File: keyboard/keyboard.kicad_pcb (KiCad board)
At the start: 2 copper layers, 214.3 x 114.3 mm, 67 parts, among them SW1 MX_SW_HS, SW10 MX_SW_HS, SW11 MX_SW_HS, SW12 MX_SW_HS, SW13 MX_SW_HS, SW14 MX_SW_HS, SW15 MX_SW_HS, SW16 MX_SW_HS, SW17 MX_SW_HS, SW18 MX_SW_HS, SW19 MX_SW_HS, SW2 MX_SW_HS, SW20 MX_SW_HS, SW21 MX_SW_HS, SW22 MX_SW_HS, SW23 MX_SW_HS, SW24 MX_SW_HS, SW25 MX_SW_HS, SW26 MX_SW_HS, SW27 MX_SW_HS, SW28 MX_SW_HS, SW29 MX_SW_HS, SW3 MX_SW_HS, SW30 MX_SW_HS, SW31 MX_SW_HS, SW32 MX_SW_HS, SW33 MX_SW_HS, SW34 MX_SW_HS, SW35 MX_SW_HS, SW36 MX_SW_HS, SW37 MX_SW_HS, SW38 MX_SW_HS, SW39 MX_SW_HS, SW4 MX_SW_HS, SW40 MX_SW_HS, SW41 MX_SW_HS, SW42 MX_SW_HS, SW43 MX_SW_HS, SW44 MX_SW_HS, SW45 MX_SW_HS, SW46 MX_SW_HS, SW47 MX_SW_HS, SW48 MX_SW_HS, SW49 MX_SW_HS, SW5 MX_SW_HS, SW50 MX_SW_HS, SW51 MX_SW_HS, SW52 MX_SW_HS, SW53 MX_SW_HS, SW54 MX_SW_HS, SW55 MX_SW_HS, SW56 MX_SW_HS, SW57 MX_SW_HS, SW58 MX_SW_HS, SW59 MX_SW_HS, SW6 MX_SW_HS, SW60 MX_SW_HS, SW61 MX_SW_HS, SW62 MX_SW_HS, SW63 MX_SW_HS, SW64 MX_SW_HS, SW7 MX_SW_HS, SW8 MX_SW_HS, SW9 MX_SW_HS, U1 ProMicro

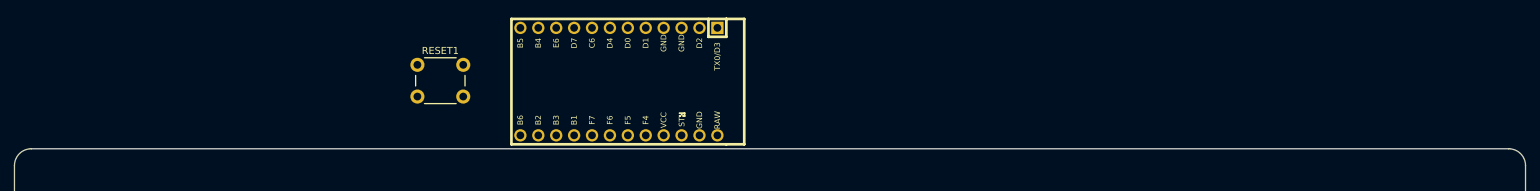
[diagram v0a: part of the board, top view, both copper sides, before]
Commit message: Add reset and cutout for the power switch
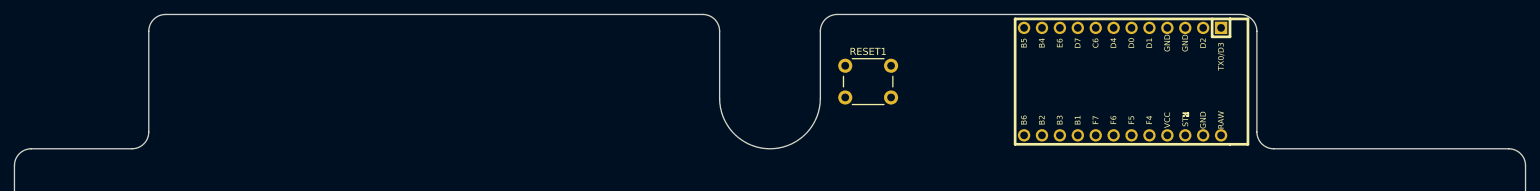
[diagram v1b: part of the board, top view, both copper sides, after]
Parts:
- moved U1 71.4 mm to (197.6, 35.7)
- moved RESET1 60.7 mm to (158.3, 33.5)
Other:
- board size 214.3 x 114.3 mm -> 214.3 x 133.3 mm
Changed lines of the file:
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@@
     )
   )
-  (footprint "Button_Switch_THT:SW_PUSH_6mm_H13mm" (layer "F.Cu")
-    (at 97.63125 33.3375)
+  (footprint "Button_Switch_THT:SW_PUSH_6mm_H13mm" locked (layer "F.Cu")
+    (at 158.309314 33.46875)
     (descr "tactile push button, 6x6mm e.g. PHAP33xx series, height=13mm")
     (tags "tact sw push 6mm")
@@
     (fp_line (start 0.25 5.25) (end 0.25 -0.75) (layer "F.Fab") (width 0.1))
     (fp_circle (center 3.25 2.25) (end 1.25 2.5) (layer "F.Fab") (width 0.1) (fill none))
-    (pad "1" thru_hole circle (at 6.5 0 90) (size 2 2) (drill 1.1) (layers *.Cu *.Mask)
+    (pad "1" thru_hole circle locked (at 6.5 0 90) (size 2 2) (drill 1.1) (layers *.Cu *.Mask)
       (net 152 "unconnected-(RESET1-Pad1)") (pinfunction "1") (pintype "passive"))
-    (pad "1" thru_hole circle (at 0 0 90) (size 2 2) (drill 1.1) (layers *.Cu *.Mask)
+    (pad "1" thru_hole circle locked (at 0 0 90) (size 2 2) (drill 1.1) (layers *.Cu *.Mask)
       (net 152 "unconnected-(RESET1-Pad1)") (pinfunction "1") (pintype "passive"))
-    (pad "2" thru_hole circle (at 6.5 4.5 90) (size 2 2) (drill 1.1) (layers *.Cu *.Mask)
+    (pad "2" thru_hole circle locked (at 6.5 4.5 90) (size 2 2) (drill 1.1) (layers *.Cu *.Mask)
       (net 153 "RESET") (pinfunction "2") (pintype "passive"))
-    (pad "2" thru_hole circle (at 0 4.5 90) (size 2 2) (drill 1.1) (layers *.Cu *.Mask)
+    (pad "2" thru_hole circle locked (at 0 4.5 90) (size 2 2) (drill 1.1) (layers *.Cu *.Mask)
       (net 153 "RESET") (pinfunction "2") (pintype "passive"))
     (model "${KICAD6_3DMODEL_DIR}/Button_Switch_THT.3dshapes/SW_PUSH_6mm_H13mm.wrl"
@@
   )
   (footprint "Keebio-Parts:ArduinoProMicro" (layer "F.Cu")
-    (at 126.20625 35.71875 180)
+    (at 197.64375 35.71875 180)
     (property "Sheetfile" "keyboard.kicad_sch")
     (property "Sheetname" "")
@@
   )
   (gr_line (start 40.48125 47.625) (end 40.48125 157.1625) (layer "Edge.Cuts") (width 0.1))
+  (gr_arc (start 59.53125 42.8625) (mid 58.833798 44.546298) (end 57.15 45.24375) (layer "Edge.Cuts") (width 0.1))
+  (gr_line (start 216.69375 42.8625) (end 216.69375 28.575) (layer "Edge.Cuts") (width 0.1))
+  (gr_arc (start 154.78125 38.1) (mid 147.6375 45.24375) (end 140.49375 38.1) (layer "Edge.Cuts") (width 0.1))
   (gr_line (start 254.79375 157.1625) (end 254.79375 47.625) (layer "Edge.Cuts") (width 0.1))
   (gr_arc (start 252.4125 45.24375) (mid 254.096283 45.941217) (end 254.79375 47.625) (layer "Edge.Cuts") (width 0.1))
@@
   (gr_arc (start 254.79375 157.1625) (mid 254.096283 158.846283) (end 252.4125 159.54375) (layer "Edge.Cuts") (width 0.1))
   (gr_arc (start 40.48125 47.625) (mid 41.178717 45.941217) (end 42.8625 45.24375) (layer "Edge.Cuts") (width 0.1))
+  (gr_line (start 140.49375 28.575) (end 140.49375 38.1) (layer "Edge.Cuts") (width 0.1))
+  (gr_line (start 214.3125 26.19375) (end 157.1625 26.19375) (layer "Edge.Cuts") (width 0.1))
+  (gr_arc (start 59.53125 28.575) (mid 60.228702 26.891202) (end 61.9125 26.19375) (layer "Edge.Cuts") (width 0.1))
+  (gr_line (start 59.53125 42.8625) (end 59.53125 28.575) (layer "Edge.Cuts") (width 0.1))
+  (gr_line (start 57.15 45.24375) (end 42.8625 45.24375) (layer "Edge.Cuts") (width 0.1))
+  (gr_arc (start 214.3125 26.19375) (mid 215.996298 26.891202) (end 216.69375 28.575) (layer "Edge.Cuts") (width 0.1))
+  (gr_line (start 61.9125 26.19375) (end 138.1125 26.19375) (layer "Edge.Cuts") (width 0.1))
+  (gr_arc (start 138.1125 26.19375) (mid 139.796298 26.891202) (end 140.49375 28.575) (layer "Edge.Cuts") (width 0.1))
+  (gr_line (start 154.78125 28.575) (end 154.78125 38.1) (layer "Edge.Cuts") (width 0.1))
   (gr_arc (start 42.8625 159.54375) (mid 41.178717 158.846283) (end 40.48125 157.1625) (layer "Edge.Cuts") (width 0.1))
-  (gr_line (start 42.8625 45.24375) (end 252.4125 45.24375) (layer "Edge.Cuts") (width 0.1))
+  (gr_arc (start 154.78125 28.575) (mid 155.478702 26.891202) (end 157.1625 26.19375) (layer "Edge.Cuts") (width 0.1))
+  (gr_arc (start 219.075 45.24375) (mid 217.391202 44.546298) (end 216.69375 42.8625) (layer "Edge.Cuts") (width 0.1))
+  (gr_line (start 219.075 45.24375) (end 252.4125 45.24375) (layer "Edge.Cuts") (width 0.1))
 )

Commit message: Switch the PCB back to a single top tab
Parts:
- moved U1 90.5 mm to (107.2, 35.7), turned to 0 degrees
- moved RESET1 50.0 mm to (208.3, 33.5)
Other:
- outline, holes or cut-outs redrawn

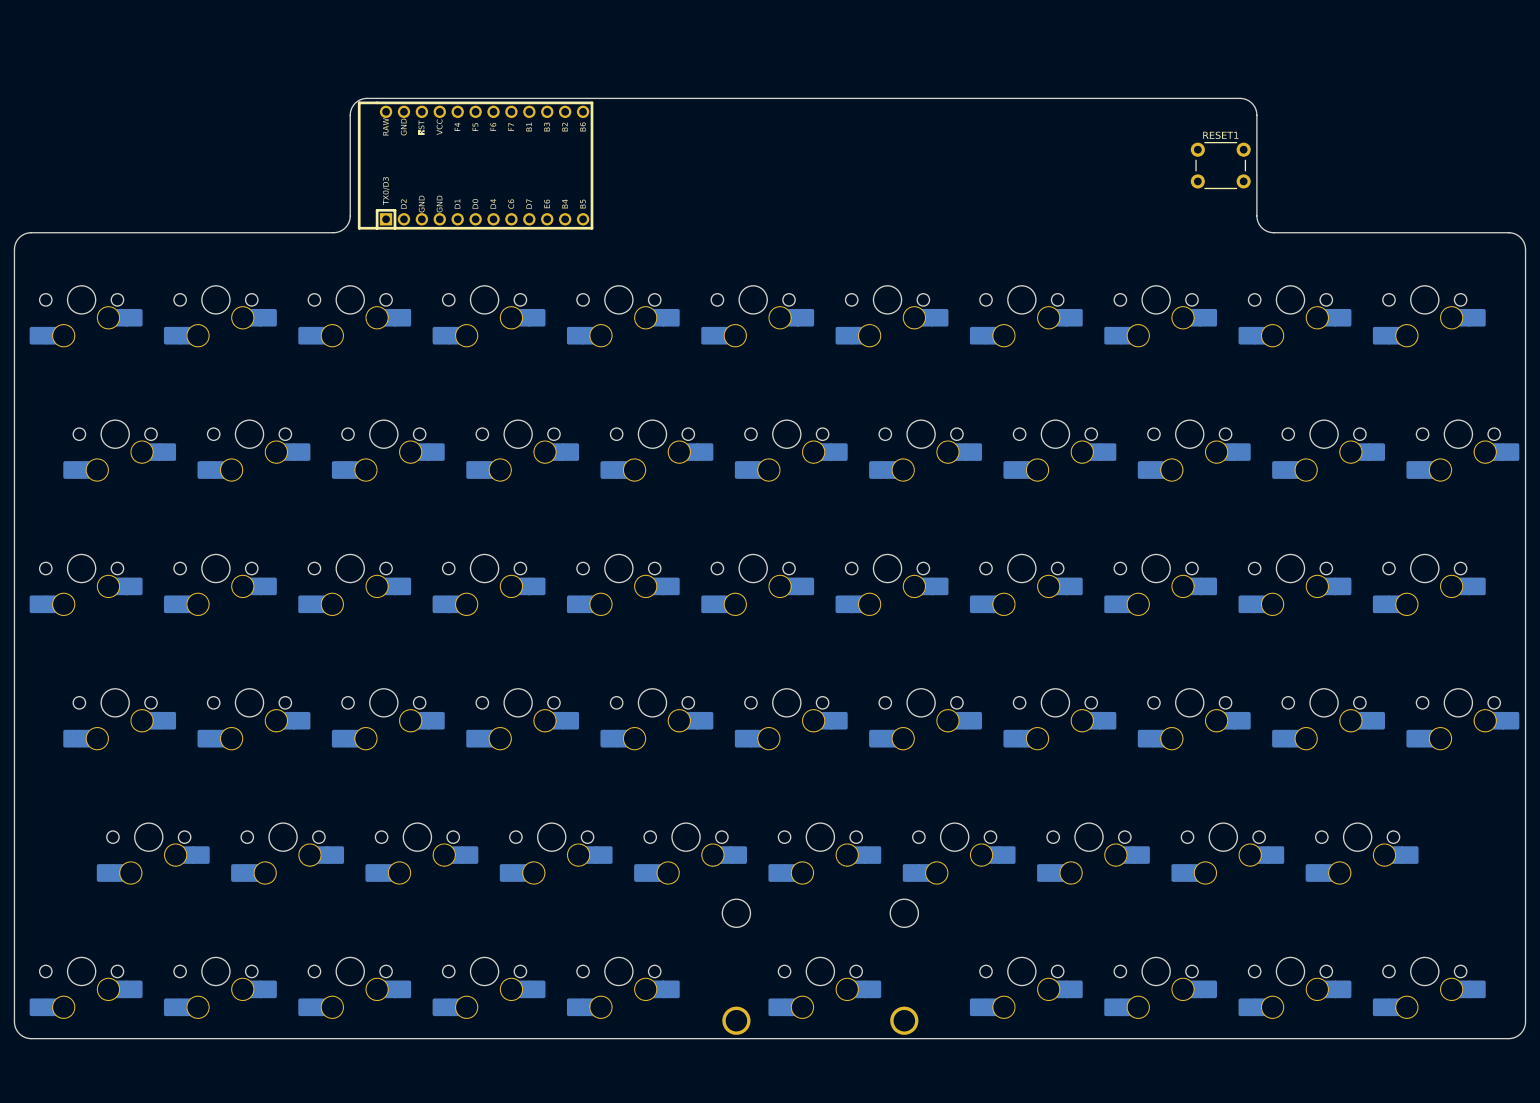
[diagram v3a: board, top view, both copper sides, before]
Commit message: First-pass diode placement
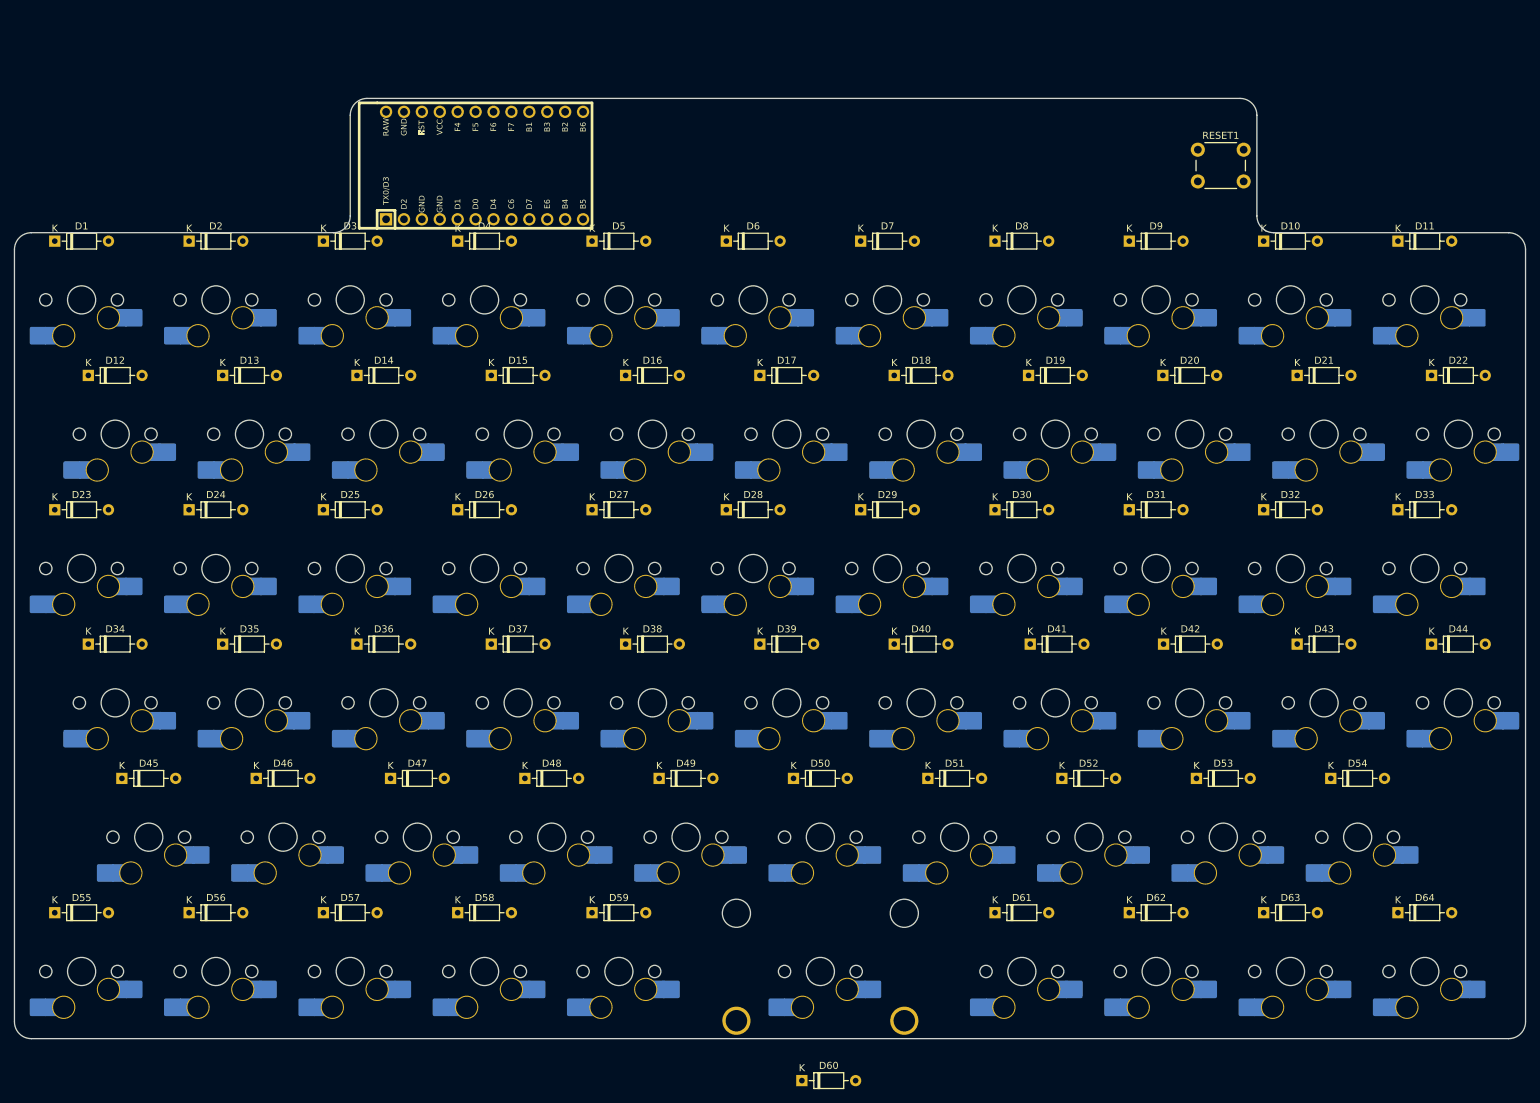
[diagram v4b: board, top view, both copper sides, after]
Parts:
- added D1: 1N4148, Diode_THT:D_DO-35_SOD27_P7.62mm_Horizontal, F.Cu at (46.2, 46.4)
- added D10: 1N4148, Diode_THT:D_DO-35_SOD27_P7.62mm_Horizontal, F.Cu at (217.6, 46.4)
- added D11: 1N4148, Diode_THT:D_DO-35_SOD27_P7.62mm_Horizontal, F.Cu at (236.7, 46.4)
- added D12: 1N4148, Diode_THT:D_DO-35_SOD27_P7.62mm_Horizontal, F.Cu at (51.0, 65.5)
- added D13: 1N4148, Diode_THT:D_DO-35_SOD27_P7.62mm_Horizontal, F.Cu at (70.0, 65.5)
- added D14: 1N4148, Diode_THT:D_DO-35_SOD27_P7.62mm_Horizontal, F.Cu at (89.1, 65.5)
- added D15: 1N4148, Diode_THT:D_DO-35_SOD27_P7.62mm_Horizontal, F.Cu at (108.1, 65.5)
- added D16: 1N4148, Diode_THT:D_DO-35_SOD27_P7.62mm_Horizontal, F.Cu at (127.2, 65.5)
- added D17: 1N4148, Diode_THT:D_DO-35_SOD27_P7.62mm_Horizontal, F.Cu at (146.2, 65.5)
- added D18: 1N4148, Diode_THT:D_DO-35_SOD27_P7.62mm_Horizontal, F.Cu at (165.3, 65.5)
- added D19: 1N4148, Diode_THT:D_DO-35_SOD27_P7.62mm_Horizontal, F.Cu at (184.3, 65.5)
- added D2: 1N4148, Diode_THT:D_DO-35_SOD27_P7.62mm_Horizontal, F.Cu at (65.2, 46.4)
- added D20: 1N4148, Diode_THT:D_DO-35_SOD27_P7.62mm_Horizontal, F.Cu at (203.4, 65.5)
- added D21: 1N4148, Diode_THT:D_DO-35_SOD27_P7.62mm_Horizontal, F.Cu at (222.4, 65.5)
- added D22: 1N4148, Diode_THT:D_DO-35_SOD27_P7.62mm_Horizontal, F.Cu at (241.5, 65.5)
- added D23: 1N4148, Diode_THT:D_DO-35_SOD27_P7.62mm_Horizontal, F.Cu at (46.2, 84.5)
- added D24: 1N4148, Diode_THT:D_DO-35_SOD27_P7.62mm_Horizontal, F.Cu at (65.2, 84.5)
- added D25: 1N4148, Diode_THT:D_DO-35_SOD27_P7.62mm_Horizontal, F.Cu at (84.3, 84.5)
- added D26: 1N4148, Diode_THT:D_DO-35_SOD27_P7.62mm_Horizontal, F.Cu at (103.3, 84.5)
- added D27: 1N4148, Diode_THT:D_DO-35_SOD27_P7.62mm_Horizontal, F.Cu at (122.4, 84.5)
- added D28: 1N4148, Diode_THT:D_DO-35_SOD27_P7.62mm_Horizontal, F.Cu at (141.4, 84.5)
- added D29: 1N4148, Diode_THT:D_DO-35_SOD27_P7.62mm_Horizontal, F.Cu at (160.5, 84.5)
- added D3: 1N4148, Diode_THT:D_DO-35_SOD27_P7.62mm_Horizontal, F.Cu at (84.3, 46.4)
- added D30: 1N4148, Diode_THT:D_DO-35_SOD27_P7.62mm_Horizontal, F.Cu at (179.5, 84.5)
- added D31: 1N4148, Diode_THT:D_DO-35_SOD27_P7.62mm_Horizontal, F.Cu at (198.6, 84.5)
- added D32: 1N4148, Diode_THT:D_DO-35_SOD27_P7.62mm_Horizontal, F.Cu at (217.6, 84.5)
- added D33: 1N4148, Diode_THT:D_DO-35_SOD27_P7.62mm_Horizontal, F.Cu at (236.7, 84.5)
- added D34: 1N4148, Diode_THT:D_DO-35_SOD27_P7.62mm_Horizontal, F.Cu at (51.0, 103.6)
- added D35: 1N4148, Diode_THT:D_DO-35_SOD27_P7.62mm_Horizontal, F.Cu at (70.0, 103.6)
- added D36: 1N4148, Diode_THT:D_DO-35_SOD27_P7.62mm_Horizontal, F.Cu at (89.1, 103.6)
- added D37: 1N4148, Diode_THT:D_DO-35_SOD27_P7.62mm_Horizontal, F.Cu at (108.1, 103.6)
- added D38: 1N4148, Diode_THT:D_DO-35_SOD27_P7.62mm_Horizontal, F.Cu at (127.2, 103.6)
- added D39: 1N4148, Diode_THT:D_DO-35_SOD27_P7.62mm_Horizontal, F.Cu at (146.2, 103.6)
- added D4: 1N4148, Diode_THT:D_DO-35_SOD27_P7.62mm_Horizontal, F.Cu at (103.3, 46.4)
- added D40: 1N4148, Diode_THT:D_DO-35_SOD27_P7.62mm_Horizontal, F.Cu at (165.3, 103.6)
- added D41: 1N4148, Diode_THT:D_DO-35_SOD27_P7.62mm_Horizontal, F.Cu at (184.5, 103.6)
- added D42: 1N4148, Diode_THT:D_DO-35_SOD27_P7.62mm_Horizontal, F.Cu at (203.5, 103.6)
- added D43: 1N4148, Diode_THT:D_DO-35_SOD27_P7.62mm_Horizontal, F.Cu at (222.4, 103.6)
- added D44: 1N4148, Diode_THT:D_DO-35_SOD27_P7.62mm_Horizontal, F.Cu at (241.5, 103.6)
- added D45: 1N4148, Diode_THT:D_DO-35_SOD27_P7.62mm_Horizontal, F.Cu at (55.7, 122.6)
- added D46: 1N4148, Diode_THT:D_DO-35_SOD27_P7.62mm_Horizontal, F.Cu at (74.8, 122.6)
- added D47: 1N4148, Diode_THT:D_DO-35_SOD27_P7.62mm_Horizontal, F.Cu at (93.8, 122.6)
- added D48: 1N4148, Diode_THT:D_DO-35_SOD27_P7.62mm_Horizontal, F.Cu at (112.9, 122.6)
- added D49: 1N4148, Diode_THT:D_DO-35_SOD27_P7.62mm_Horizontal, F.Cu at (131.9, 122.6)
- added D5: 1N4148, Diode_THT:D_DO-35_SOD27_P7.62mm_Horizontal, F.Cu at (122.4, 46.4)
- added D50: 1N4148, Diode_THT:D_DO-35_SOD27_P7.62mm_Horizontal, F.Cu at (151.0, 122.6)
- added D51: 1N4148, Diode_THT:D_DO-35_SOD27_P7.62mm_Horizontal, F.Cu at (170.0, 122.6)
- added D52: 1N4148, Diode_THT:D_DO-35_SOD27_P7.62mm_Horizontal, F.Cu at (189.0, 122.6)
- added D53: 1N4148, Diode_THT:D_DO-35_SOD27_P7.62mm_Horizontal, F.Cu at (208.1, 122.6)
- added D54: 1N4148, Diode_THT:D_DO-35_SOD27_P7.62mm_Horizontal, F.Cu at (227.2, 122.6)
- added D55: 1N4148, Diode_THT:D_DO-35_SOD27_P7.62mm_Horizontal, F.Cu at (46.2, 141.7)
- added D56: 1N4148, Diode_THT:D_DO-35_SOD27_P7.62mm_Horizontal, F.Cu at (65.2, 141.7)
- added D57: 1N4148, Diode_THT:D_DO-35_SOD27_P7.62mm_Horizontal, F.Cu at (84.3, 141.7)
- added D58: 1N4148, Diode_THT:D_DO-35_SOD27_P7.62mm_Horizontal, F.Cu at (103.3, 141.7)
- added D59: 1N4148, Diode_THT:D_DO-35_SOD27_P7.62mm_Horizontal, F.Cu at (122.4, 141.7)
- added D6: 1N4148, Diode_THT:D_DO-35_SOD27_P7.62mm_Horizontal, F.Cu at (141.4, 46.4)
- added D60: 1N4148, Diode_THT:D_DO-35_SOD27_P7.62mm_Horizontal, F.Cu at (152.2, 165.5)
- added D61: 1N4148, Diode_THT:D_DO-35_SOD27_P7.62mm_Horizontal, F.Cu at (179.5, 141.7)
- added D62: 1N4148, Diode_THT:D_DO-35_SOD27_P7.62mm_Horizontal, F.Cu at (198.6, 141.7)
- added D63: 1N4148, Diode_THT:D_DO-35_SOD27_P7.62mm_Horizontal, F.Cu at (217.6, 141.7)
- added D64: 1N4148, Diode_THT:D_DO-35_SOD27_P7.62mm_Horizontal, F.Cu at (236.7, 141.7)
- added D7: 1N4148, Diode_THT:D_DO-35_SOD27_P7.62mm_Horizontal, F.Cu at (160.5, 46.4)
- added D8: 1N4148, Diode_THT:D_DO-35_SOD27_P7.62mm_Horizontal, F.Cu at (179.5, 46.4)
- added D9: 1N4148, Diode_THT:D_DO-35_SOD27_P7.62mm_Horizontal, F.Cu at (198.6, 46.4)
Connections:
- SW1 pad 1: unconnected-(SW1-Pad1) -> Net-(D1-Pad2)
- SW10 pad 1: unconnected-(SW10-Pad1) -> Net-(D10-Pad2)
- SW11 pad 1: unconnected-(SW11-Pad1) -> Net-(SW11-Pad1)
- SW12 pad 1: unconnected-(SW12-Pad1) -> Net-(SW12-Pad1)
- SW13 pad 1: unconnected-(SW13-Pad1) -> Net-(SW13-Pad1)
- SW14 pad 1: unconnected-(SW14-Pad1) -> Net-(D14-Pad2)
- SW15 pad 1: unconnected-(SW15-Pad1) -> Net-(D15-Pad2)
- SW16 pad 1: unconnected-(SW16-Pad1) -> Net-(SW16-Pad1)
- SW17 pad 1: unconnected-(SW17-Pad1) -> Net-(SW17-Pad1)
- SW18 pad 1: unconnected-(SW18-Pad1) -> Net-(SW18-Pad1)
- SW19 pad 1: unconnected-(SW19-Pad1) -> Net-(D19-Pad2)
- SW2 pad 1: unconnected-(SW2-Pad1) -> Net-(D2-Pad2)
- SW20 pad 1: unconnected-(SW20-Pad1) -> Net-(D20-Pad2)
- SW21 pad 1: unconnected-(SW21-Pad1) -> Net-(D21-Pad2)
- SW22 pad 1: unconnected-(SW22-Pad1) -> Net-(SW22-Pad1)
- SW23 pad 1: unconnected-(SW23-Pad1) -> Net-(SW23-Pad1)
- SW24 pad 1: unconnected-(SW24-Pad1) -> Net-(SW24-Pad1)
- SW25 pad 1: unconnected-(SW25-Pad1) -> Net-(SW25-Pad1)
- SW26 pad 1: unconnected-(SW26-Pad1) -> Net-(SW26-Pad1)
- SW27 pad 1: unconnected-(SW27-Pad1) -> Net-(SW27-Pad1)
- SW28 pad 1: unconnected-(SW28-Pad1) -> Net-(D28-Pad2)
- SW29 pad 1: unconnected-(SW29-Pad1) -> Net-(SW29-Pad1)
- SW3 pad 1: unconnected-(SW3-Pad1) -> Net-(D3-Pad2)
- SW30 pad 1: unconnected-(SW30-Pad1) -> Net-(D30-Pad2)
- SW31 pad 1: unconnected-(SW31-Pad1) -> Net-(SW31-Pad1)
- SW32 pad 1: unconnected-(SW32-Pad1) -> Net-(D32-Pad2)
- SW33 pad 1: unconnected-(SW33-Pad1) -> Net-(D33-Pad2)
- SW34 pad 1: unconnected-(SW34-Pad1) -> Net-(SW34-Pad1)
- SW35 pad 1: unconnected-(SW35-Pad1) -> Net-(D35-Pad2)
- SW36 pad 1: unconnected-(SW36-Pad1) -> Net-(SW36-Pad1)
- SW37 pad 1: unconnected-(SW37-Pad1) -> Net-(SW37-Pad1)
- SW38 pad 1: unconnected-(SW38-Pad1) -> Net-(SW38-Pad1)
- SW39 pad 1: unconnected-(SW39-Pad1) -> Net-(SW39-Pad1)
- SW4 pad 1: unconnected-(SW4-Pad1) -> Net-(D4-Pad2)
- SW40 pad 1: unconnected-(SW40-Pad1) -> Net-(SW40-Pad1)
- SW41 pad 1: unconnected-(SW41-Pad1) -> Net-(SW41-Pad1)
- SW42 pad 1: unconnected-(SW42-Pad1) -> Net-(SW42-Pad1)
- SW43 pad 1: unconnected-(SW43-Pad1) -> Net-(D43-Pad2)
- SW44 pad 1: unconnected-(SW44-Pad1) -> Net-(SW44-Pad1)
- SW45 pad 1: unconnected-(SW45-Pad1) -> Net-(SW45-Pad1)
- SW46 pad 1: unconnected-(SW46-Pad1) -> Net-(SW46-Pad1)
- SW47 pad 1: unconnected-(SW47-Pad1) -> Net-(SW47-Pad1)
- SW48 pad 1: unconnected-(SW48-Pad1) -> Net-(SW48-Pad1)
- SW49 pad 1: unconnected-(SW49-Pad1) -> Net-(SW49-Pad1)
- SW5 pad 1: unconnected-(SW5-Pad1) -> Net-(SW5-Pad1)
- SW50 pad 1: unconnected-(SW50-Pad1) -> Net-(SW50-Pad1)
- SW51 pad 1: unconnected-(SW51-Pad1) -> Net-(SW51-Pad1)
- SW52 pad 1: unconnected-(SW52-Pad1) -> Net-(SW52-Pad1)
- SW53 pad 1: unconnected-(SW53-Pad1) -> Net-(SW53-Pad1)
- SW54 pad 1: unconnected-(SW54-Pad1) -> Net-(SW54-Pad1)
- SW55 pad 1: unconnected-(SW55-Pad1) -> Net-(SW55-Pad1)
- SW56 pad 1: unconnected-(SW56-Pad1) -> Net-(SW56-Pad1)
- SW57 pad 1: unconnected-(SW57-Pad1) -> Net-(D57-Pad2)
- SW58 pad 1: unconnected-(SW58-Pad1) -> Net-(SW58-Pad1)
- SW59 pad 1: unconnected-(SW59-Pad1) -> Net-(SW59-Pad1)
- SW6 pad 1: unconnected-(SW6-Pad1) -> Net-(D6-Pad2)
- SW60 pad 1: unconnected-(SW60-Pad1) -> Net-(SW60-Pad1)
- SW61 pad 1: unconnected-(SW61-Pad1) -> Net-(SW61-Pad1)
- SW62 pad 1: unconnected-(SW62-Pad1) -> Net-(SW62-Pad1)
- SW63 pad 1: unconnected-(SW63-Pad1) -> Net-(SW63-Pad1)
- SW64 pad 1: unconnected-(SW64-Pad1) -> Net-(SW64-Pad1)
- SW7 pad 1: unconnected-(SW7-Pad1) -> Net-(SW7-Pad1)
- SW8 pad 1: unconnected-(SW8-Pad1) -> Net-(SW8-Pad1)
- SW9 pad 1: unconnected-(SW9-Pad1) -> Net-(D9-Pad2)

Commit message: Place the spacebar diode
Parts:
- moved D60 28.1 mm to (172.6, 146.2), turned to -90 degrees
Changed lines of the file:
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@@
   )
   (footprint "Diode_THT:D_DO-35_SOD27_P7.62mm_Horizontal" (layer "F.Cu")
-    (at 152.161875 165.496875)
+    (at 172.640625 146.20875 -90)
     (descr "Diode, DO-35_SOD27 series, Axial, Horizontal, pin pitch=7.62mm, , length*diameter=4*2mm^2, , http://www.diodes.com/_files/packages/DO-35.pdf")
     (tags "Diode DO-35_SOD27 series Axial Horizontal pin pitch 7.62mm  length 4mm diameter 2mm")
@@
     (property "Sheetname" "")
     (attr through_hole)
-    (fp_text reference "D60" (at 3.81 -2.12) (layer "F.SilkS")
+    (fp_text reference "D60" (at 3.81 -2.12 90) (layer "F.SilkS")
       (effects (font (size 1 1) (thickness 0.15)))
     )
-    (fp_text value "1N4148" (at 3.81 2.12) (layer "F.Fab")
+    (fp_text value "1N4148" (at 3.81 2.12 90) (layer "F.Fab")
       (effects (font (size 1 1) (thickness 0.15)))
     )
-    (fp_text user "K" (at 0 -1.8) (layer "F.SilkS")
+    (fp_text user "K" (at 0 -1.8 90) (layer "F.SilkS")
       (effects (font (size 1 1) (thickness 0.15)))
     )
-    (fp_text user "${REFERENCE}" (at 4.11 0) (layer "F.Fab")
+    (fp_text user "${REFERENCE}" (at 4.11 0 90) (layer "F.Fab")
       (effects (font (size 0.8 0.8) (thickness 0.12)))
     )
-    (fp_text user "K" (at 0 -1.8) (layer "F.Fab")
+    (fp_text user "K" (at 0 -1.8 90) (layer "F.Fab")
       (effects (font (size 1 1) (thickness 0.15)))
     )
@@
     (fp_line (start 1.81 -1) (end 1.81 1) (layer "F.Fab") (width 0.1))
     (fp_line (start 7.62 0) (end 5.81 0) (layer "F.Fab") (width 0.1))
-    (pad "1" thru_hole rect (at 0 0) (size 1.6 1.6) (drill 0.8) (layers *.Cu *.Mask)
+    (pad "1" thru_hole rect (at 0 0 270) (size 1.6 1.6) (drill 0.8) (layers *.Cu *.Mask)
       (net 206 "unconnected-(D60-Pad1)") (pinfunction "K") (pintype "passive"))
-    (pad "2" thru_hole oval (at 7.62 0) (size 1.6 1.6) (drill 0.8) (layers *.Cu *.Mask)
+    (pad "2" thru_hole oval (at 7.62 0 270) (size 1.6 1.6) (drill 0.8) (layers *.Cu *.Mask)
       (net 207 "Net-(SW60-Pad1)") (pinfunction "A") (pintype "passive"))
     (model "${KICAD6_3DMODEL_DIR}/Diode_THT.3dshapes/D_DO-35_SOD27_P7.62mm_Horizontal.wrl"
